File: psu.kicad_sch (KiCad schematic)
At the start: 38 parts, among them J3 Screw_Terminal_01x03, J4 Screw_Terminal_01x02, U15 AP1117-ADJ, U17 AP1117-ADJ, U18 AP1117-ADJ, U19 AP1117-ADJ, U20 AP1117-ADJ

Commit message: Finished schematic?
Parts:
- removed C24, C28, C29, C51: C, symbol Device:C
- removed C26: 22uF, symbol Device:C
- removed C30, C31, C32: 10uF, symbol Device:C
- removed R65, R66, R69, R70, R71, R72: R, Resistor_SMD:R_1206_3216Metric, symbol Device:R
- removed U17, U19, U20: AP1117-ADJ, Package_TO_SOT_SMD:SOT-223-3_TabPin2, symbol Regulator_Linear:AP1117-ADJ
- added C24, C32, C51: 10uF, symbol Device:C_Polarized
- added C65, C68, C70: 10uF, symbol Device:C
- added C67, C69: 100nF, symbol Device:C
- added L1, L11, L5: 0.68uH, 0.8Ohm, symbol Device:L
- added L12, L2, L6: LCBB-601, symbol Device:L
- added R203: 240, Resistor_SMD:R_1206_3216Metric, symbol Device:R
- added R204: 430, Resistor_SMD:R_1206_3216Metric, symbol Device:R
- added U22: AP1117-ADJ, Package_TO_SOT_SMD:SOT-223-3_TabPin2, symbol Regulator_Linear:AP1117-ADJ
- C27: value C -> 100nF
- C48: value 22uF -> 10uF
- C49, C50, C53: value 22uF -> 100nF
- R67: value R -> 120
- R68: value R -> 200
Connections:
- net +12V: now also L1.1
- net +5V: now also L5.1; no longer C27.1, C52.1, U18.3 (VI)
- net -5V: now also L11.1
- net GND: now also C24.2, C32.2, C51.2, C65.2, C67.2, C68.2, C69.2, C70.2, R204.2
- net at C50.1: now also C48.1, C32.1, L12.2, U22.3 (VI)
- net at C53.1: now also C52.1, U15.3 (VI), C51.1, L2.2
- net +6V5: now reaches R50.1, U15.2 (VO)
- net +6V5: now also C69.1, C70.1
- net +3V3: now reaches C49.1, R67.1, U18.2 (VO)
- net +3V3: now also C65.1
- net +9V: no longer names the net of C25.1
- net +9V: now also C27.1, U18.3 (VI), C24.1, L6.2; no longer U15.3 (VI)
- new net: L5.2, L6.1
- new net: R203.2, R204.1, U22.1 (ADJ)
- new net: L11.2, L12.1
- new net: L1.2, L2.1
- new net -3V5: C67.1, C68.1, R203.1, U22.2 (VO)
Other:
- note removed: "TODO: recommended to change for AZ1117C/E"
- moved on the sheet: D3, D4, D5, J3, J4, R50, R52, R61, R62, R76, U15

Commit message: Almost finishing schematic
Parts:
- added C31: 10uF, symbol Device:C_Polarized
- added C62, C66: 10uF, symbol Device:C
- added C63, C64: 100nF, symbol Device:C
- added L3: 0.68uH, 0.8Ohm, symbol Device:L
- added L4: LCBB-601, symbol Device:L
- added R65: 120, Resistor_SMD:R_1206_3216Metric, symbol Device:R
- added R66: 200, Resistor_SMD:R_1206_3216Metric, symbol Device:R
- added U2: AP1117-ADJ, Package_TO_SOT_SMD:SOT-223-3_TabPin2, symbol Regulator_Linear:AP1117-ADJ
- R61, R62: value 5K1 -> 1k2
- R76: value 12K -> 600
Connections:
- net +5V: now also C64.1, C66.1, R65.1, U2.2 (VO); no longer D4.2 (A), J3.1 (Pin_1), L5.1
- net GND: now also C31.2, C62.2, C63.2, C64.2, C66.2, R66.2
- net +12V renamed +5V_EXT
- net +5V_EXT: no longer L1.1
- net -5V renamed -8V
- new net: L3.2, L4.1
- new net: C31.1, C62.1, C63.1, L4.2, U2.3 (VI)
- new net: R65.2, R66.1, U2.1 (ADJ)
- new net +8V: D4.2 (A), J3.1 (Pin_1), L1.1, L3.1
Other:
- note added: "+5V_EXT"
- note added: "+8V / -8V"
- note added: "External power"
- note removed: "+5V / -5V"
- note removed: "12V"
- moved on the sheet: C24, C25, C27, C32, C48, C49, C50, C51, C52, C53, C65, C67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

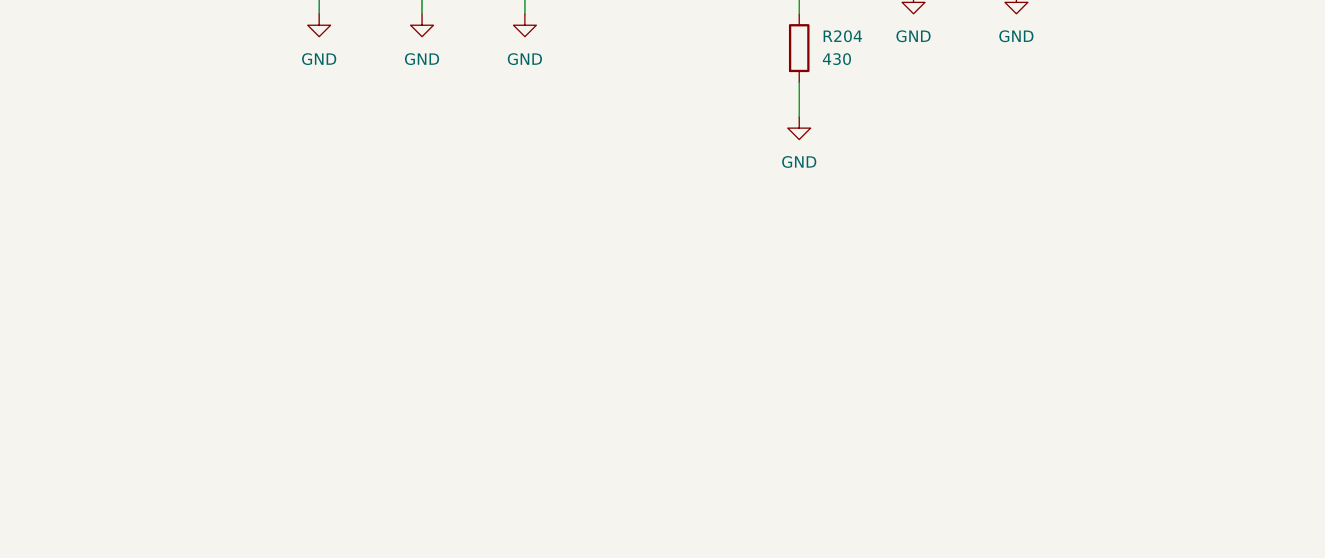
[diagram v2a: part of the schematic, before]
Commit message: Save work before deleting amps from DAC to offset
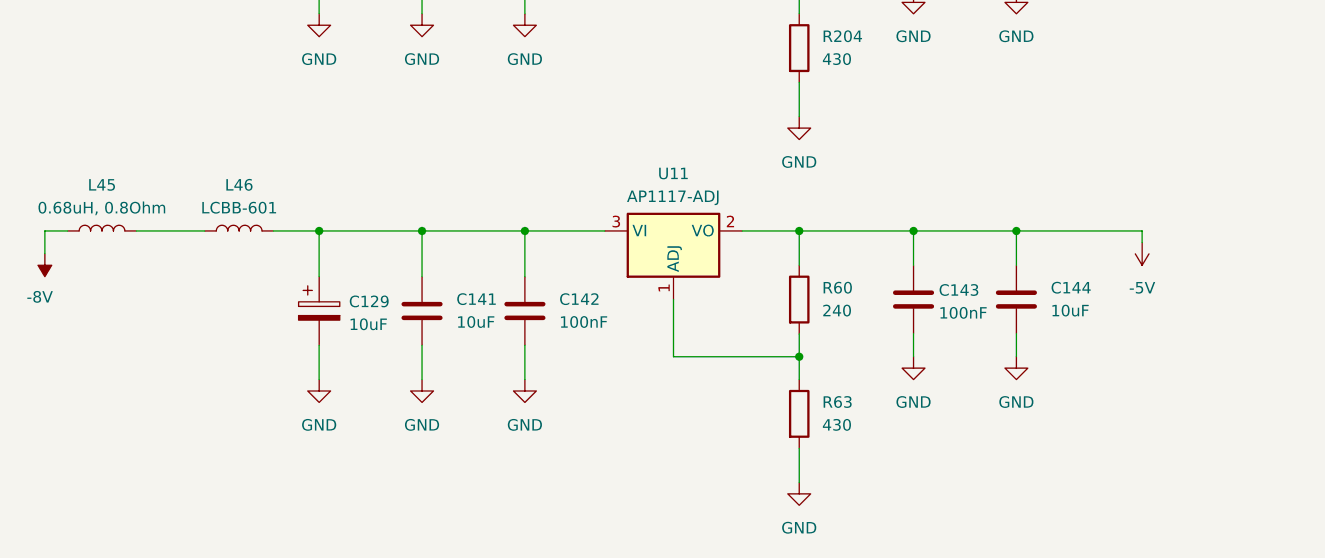
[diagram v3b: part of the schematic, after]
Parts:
- added C129: 10uF, symbol Device:C_Polarized
- added C141, C144: 10uF, symbol Device:C
- added C142, C143: 100nF, symbol Device:C
- added L45: 0.68uH, 0.8Ohm, symbol Device:L
- added L46: LCBB-601, symbol Device:L
- added R60: 240, Resistor_SMD:R_1206_3216Metric, symbol Device:R
- added R63: 430, Resistor_SMD:R_1206_3216Metric, symbol Device:R
- added U11: AP1117-ADJ, Package_TO_SOT_SMD:SOT-223-3_TabPin2, symbol Regulator_Linear:AP1117-ADJ
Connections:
- net -8V: now also L45.1
- net GND: now also C129.2, C141.2, C142.2, C143.2, C144.2, R63.2
- new net: L45.2, L46.1
- new net: R60.2, R63.1, U11.1 (ADJ)
- new net: C129.1, C141.1, C142.1, L46.2, U11.3 (VI)
- new net -5V: C143.1, C144.1, R60.1, U11.2 (VO)

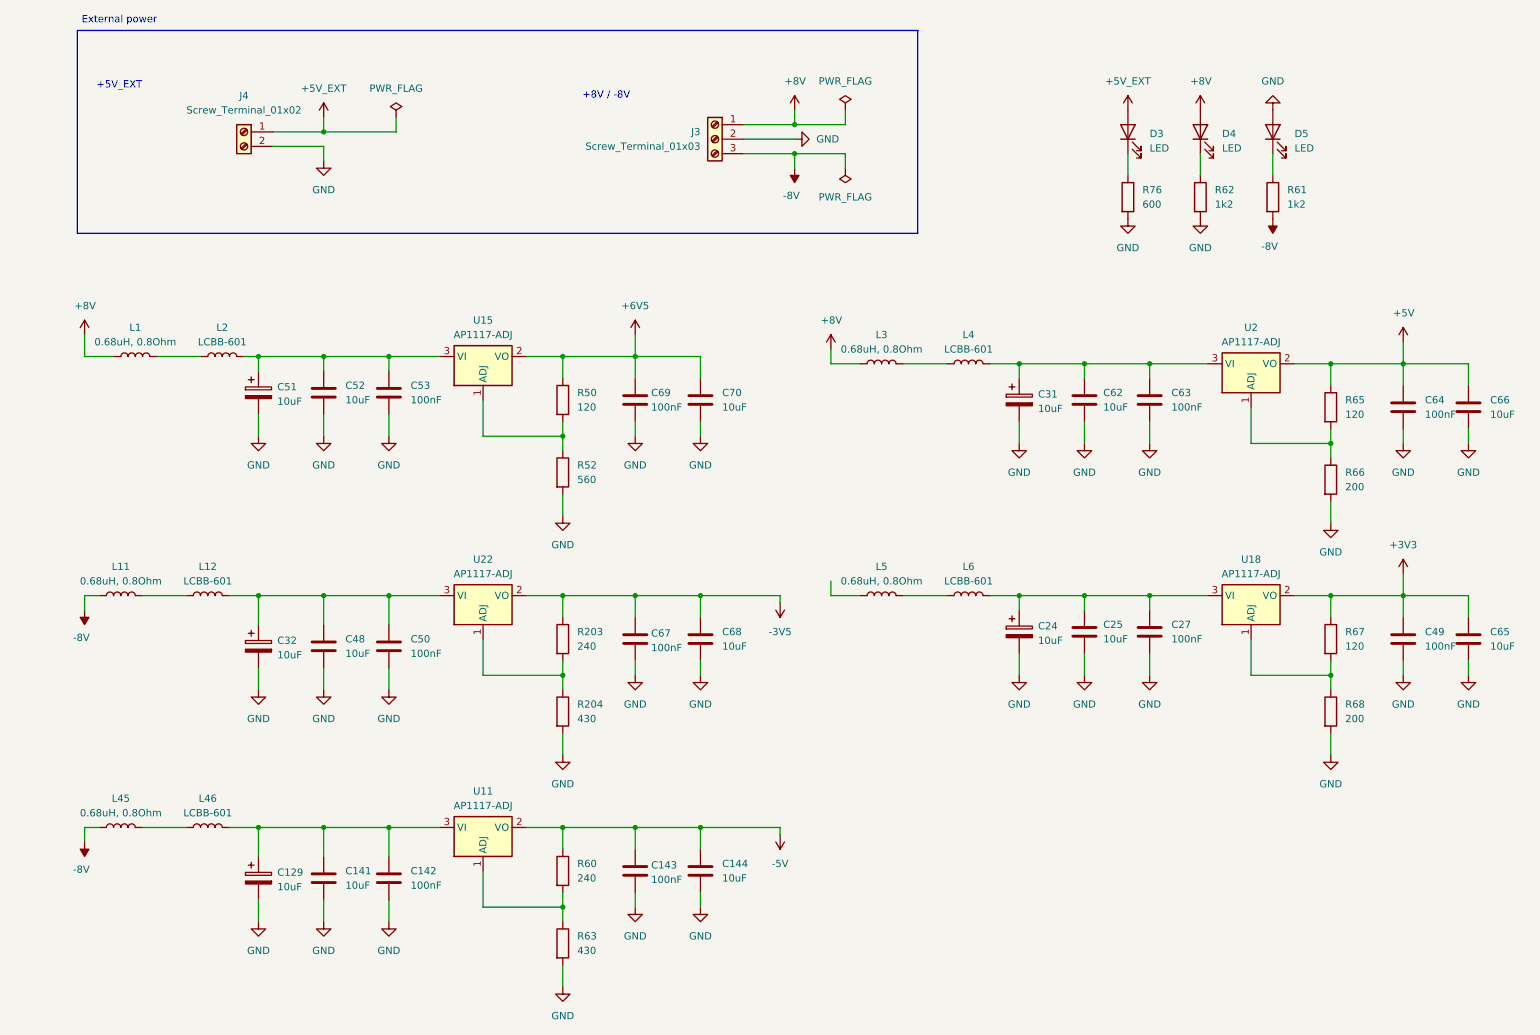
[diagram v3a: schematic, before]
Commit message: Save work, I don't think we throw out the 2x amps
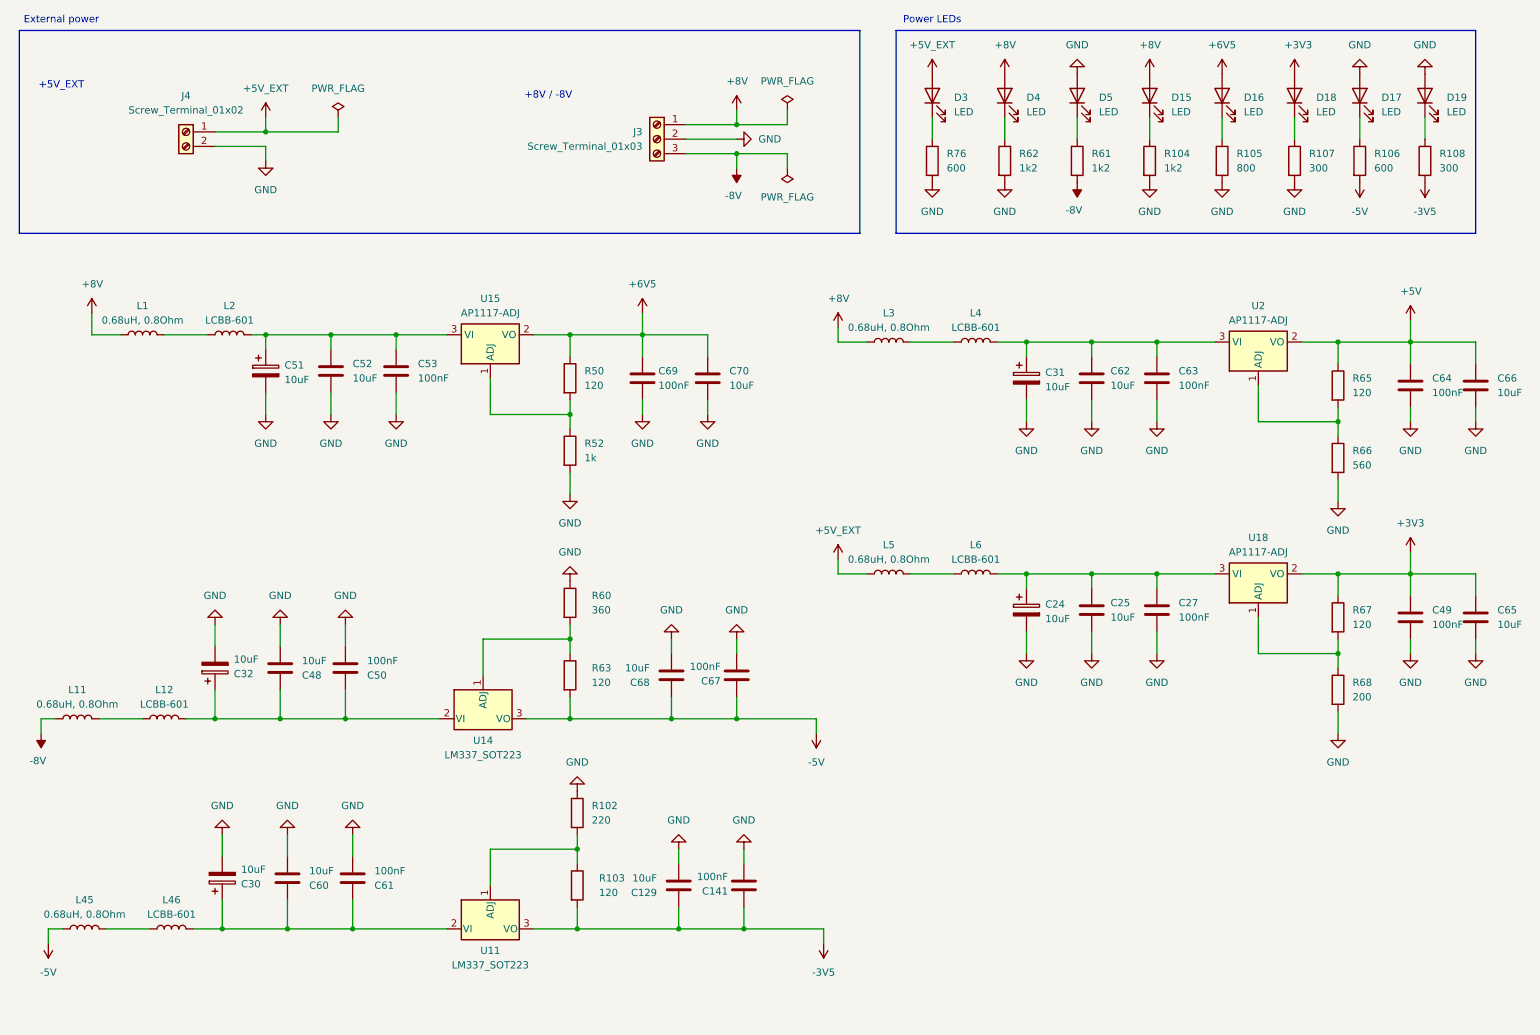
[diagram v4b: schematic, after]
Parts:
- removed C129: 10uF, symbol Device:C_Polarized
- removed C142, C143: 100nF, symbol Device:C
- removed C144: 10uF, symbol Device:C
- removed R203: 240, Resistor_SMD:R_1206_3216Metric, symbol Device:R
- removed R204: 430, Resistor_SMD:R_1206_3216Metric, symbol Device:R
- removed U11, U22: AP1117-ADJ, Package_TO_SOT_SMD:SOT-223-3_TabPin2, symbol Regulator_Linear:AP1117-ADJ
- added C129, C60: 10uF, symbol Device:C
- added C30: 10uF, symbol Device:C_Polarized
- added C61: 100nF, symbol Device:C
- added D15, D16, D17, D18, D19: LED, symbol Device:LED
- added R102: 220, Resistor_SMD:R_1206_3216Metric, symbol Device:R
- added R103: 120, Resistor_SMD:R_1206_3216Metric, symbol Device:R
- added R104: 1k2, Resistor_SMD:R_1206_3216Metric, symbol Device:R
- added R105: 800, Resistor_SMD:R_1206_3216Metric, symbol Device:R
- added R106: 600, Resistor_SMD:R_1206_3216Metric, symbol Device:R
- added R107, R108: 300, Resistor_SMD:R_1206_3216Metric, symbol Device:R
- added U11, U14: LM337_SOT223, Package_TO_SOT_SMD:SOT-223-3_TabPin2, symbol Regulator_Linear:LM337_SOT223
- C141: value 10uF -> 100nF
- R52: value 560 -> 1k
- R60: value 240 -> 360
- R63: value 430 -> 120
- R66: value 200 -> 560
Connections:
- net +3V3: now also D18.2 (A)
- net +5V_EXT: now also L5.1
- net +6V5: now also D16.2 (A)
- net +8V: now also D15.2 (A)
- net -3V5: now also C141.1, C129.1, R103.2, R108.2, U11.3 (VO); no longer C67.1, C68.1
- net -5V: now also C67.1, C68.1, L45.1, R63.2, R106.2, U14.3 (VO); no longer R60.1
- net -8V: no longer L45.1
- net GND: now also R60.1, C129.2, C30.2, C60.2, C61.2, D17.2 (A), D19.2 (A), R102.1, R104.2, R105.2, R107.2; no longer R63.2
- net at C32.1, C48.1, C50.1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: now also U14.2 (VI)
- net at R60.2, R63.1: now also U14.1 (ADJ)
- net at L46.2: now also C30.1, C60.1, C61.1, U11.2 (VI); no longer C141.1
- new net: D19.1 (K), R108.1
- new net: D18.1 (K), R107.1
- new net: R102.2, R103.1, U11.1 (ADJ)
- new net: D15.1 (K), R104.1
- new net: D16.1 (K), R105.1
- new net: D17.1 (K), R106.1
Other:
- note added: "Power LEDs"
- moved on the sheet: C24, C25, C27, C31, C32, C48, C49, C50, C51, C52, C53, C62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
